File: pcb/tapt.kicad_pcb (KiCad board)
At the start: 2 copper layers, 23.7 x 28.3 mm, 26 parts, among them SW1 SW_SPDT_XKB_DMx-xxxx-1, SW2 SW_SPST, U1 nRF52810-QCxx, Y1 32MHz

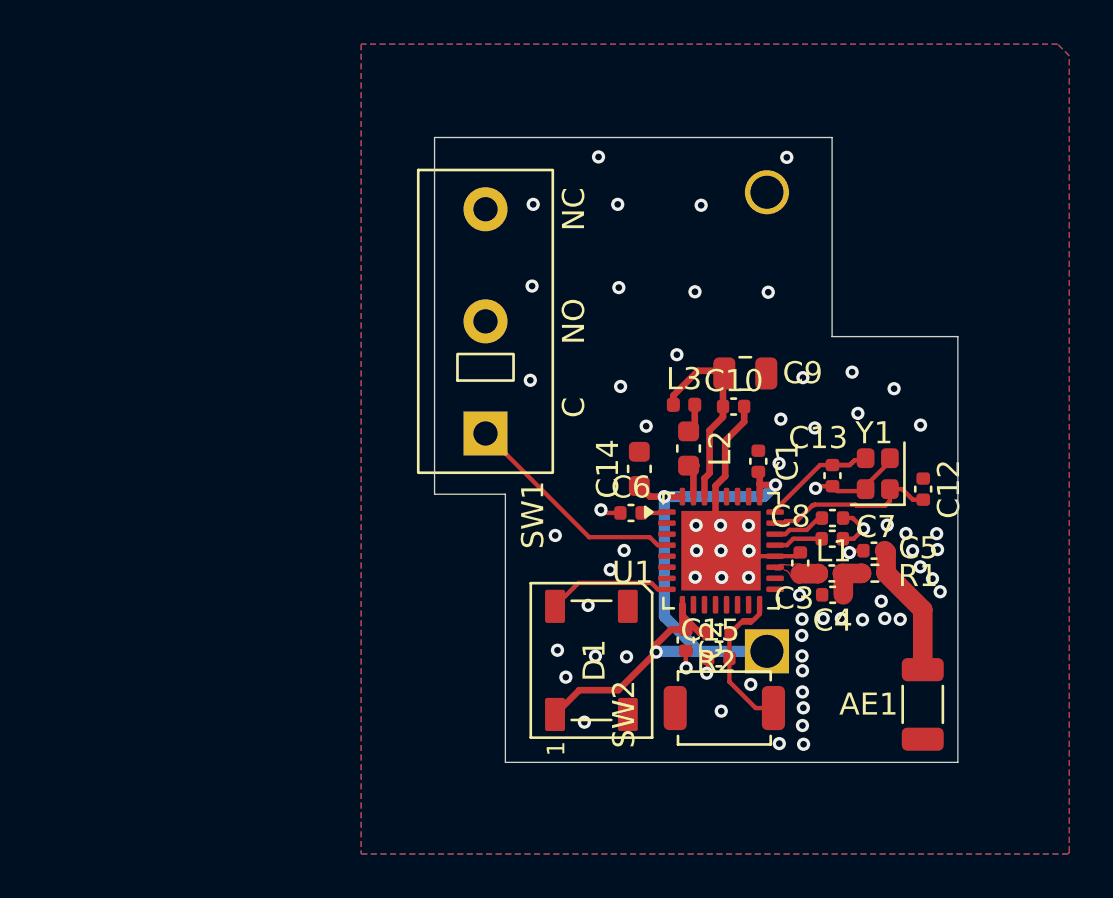
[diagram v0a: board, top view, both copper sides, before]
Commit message: major rf improvements, battery connector, component relayout
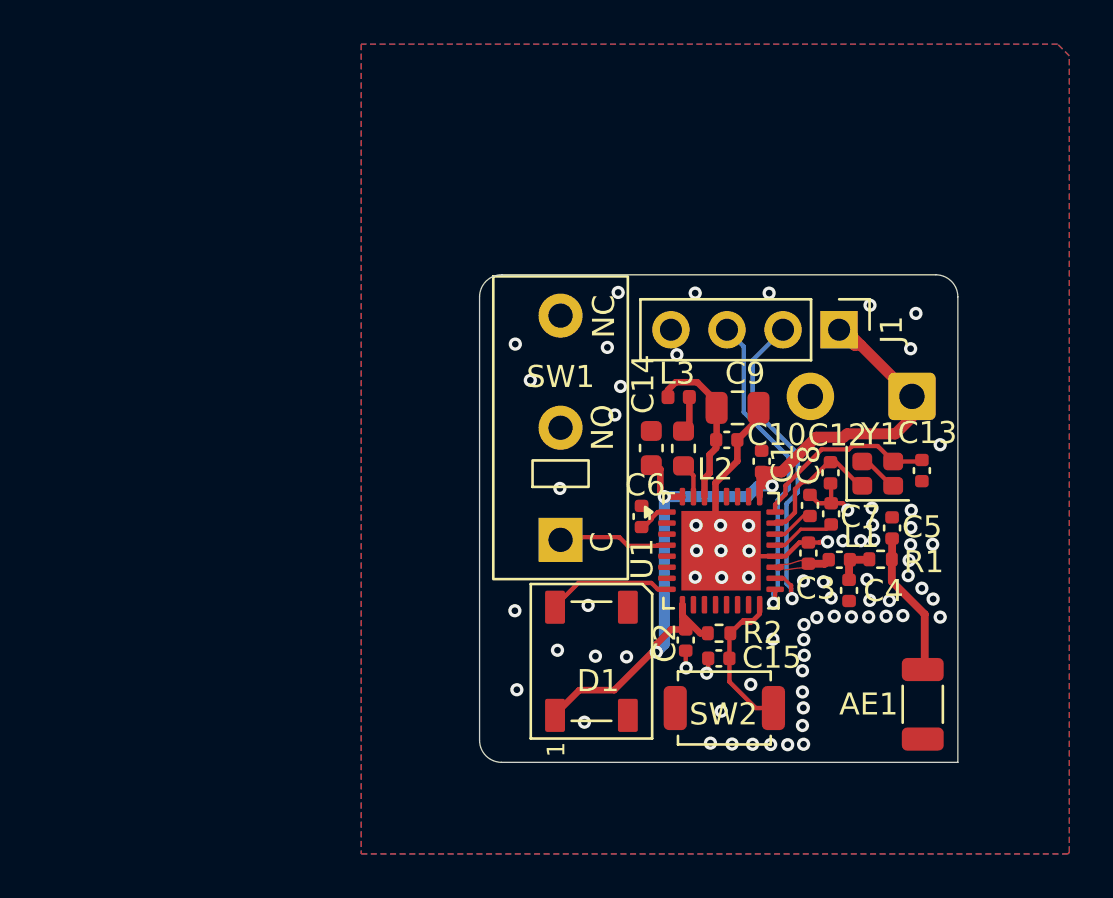
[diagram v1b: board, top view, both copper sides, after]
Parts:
- added J1: Conn_01x04_Pin, Connector_PinHeader_2.54mm:PinHeader_1x04_P2.54mm_Vertical, F.Cu at (103.5, 62.9)
- BT1: footprint Battery:BatteryHolder_MYOUNG_BS-07-A1BJ001_CR2032 -> Connector_Wire:SolderWire-0.5sqmm_1x02_P4.6mm_D0.9mm_OD2.1mm
- L2: footprint Capacitor_SMD:C_0603_1608Metric -> Inductor_SMD:L_0603_1608Metric
- moved BT1 13.3 mm to (106.8, 65.9), turned to 180 degrees
- moved SW1 5.90 mm to (90.8, 72.4)
- moved C12 4.26 mm to (103.1, 69.3), turned to 90 degrees
- moved C13 4.06 mm to (107.2, 69.2)
- moved C9 1.60 mm to (98.8, 66.4)
- moved C10 1.54 mm to (98.4, 67.8)
- moved C5 1.32 mm to (105.8, 71.8), turned to 90 degrees
- moved C8 1.17 mm to (102.1, 70.8), turned to -90 degrees
- moved C7 1.13 mm to (103.1, 71.2), turned to -90 degrees
- moved C14 1.09 mm to (94.9, 68.2)
- moved C4 0.77 mm to (103.9, 74.7), turned to -90 degrees
- moved L1 0.71 mm to (103.5, 73.3)
- moved R1 0.68 mm to (105.3, 73.3)
- moved C3 0.58 mm to (102.1, 73.0)
- moved C6 0.51 mm to (94.5, 71.3), turned to -90 degrees
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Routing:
- net SWDIO: track 0.00 -> 15.4 mm, vias 0 -> 1
- net SWDCLK: track 0.00 -> 14.5 mm, vias 0 -> 1
- net VDD: track 33.6 -> 42.6 mm
- net LIMIT: track 10.3 -> 5.85 mm
- net Net-(U1-XC2): track 5.91 -> 8.64 mm
- net GND: track 20.8 -> 19.0 mm, vias 71 -> 76
- net Net-(U1-XC1): track 7.94 -> 6.26 mm
- net Net-(U1-DEC4): track 9.17 -> 7.57 mm
- net Net-(U1-DEC2): track 2.23 -> 2.93 mm
- net Net-(AE1-FEED): track 5.99 -> 6.65 mm
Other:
- board size 23.7 x 28.3 mm -> 21.7 x 22.1 mm

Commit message: add mounting holes on dogboned corners
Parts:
- added H1: MountingHole, MountingHole:MountingHole_2.7mm_M2.5, F.Cu at (86.8, 82.5)
- added H2: MountingHole, MountingHole:MountingHole_2.7mm_M2.5, F.Cu at (108.8, 60.5)
- moved D1 0.28 mm to (92.2, 77.6)
- moved SW1 0.27 mm to (90.8, 72.1)
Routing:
- net GND: track 19.0 -> 23.2 mm, vias 76 -> 89
- net VDD: track 42.6 -> 42.0 mm, vias 3 -> 4
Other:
- board size 21.7 x 22.1 mm -> 28.3 x 28.3 mm

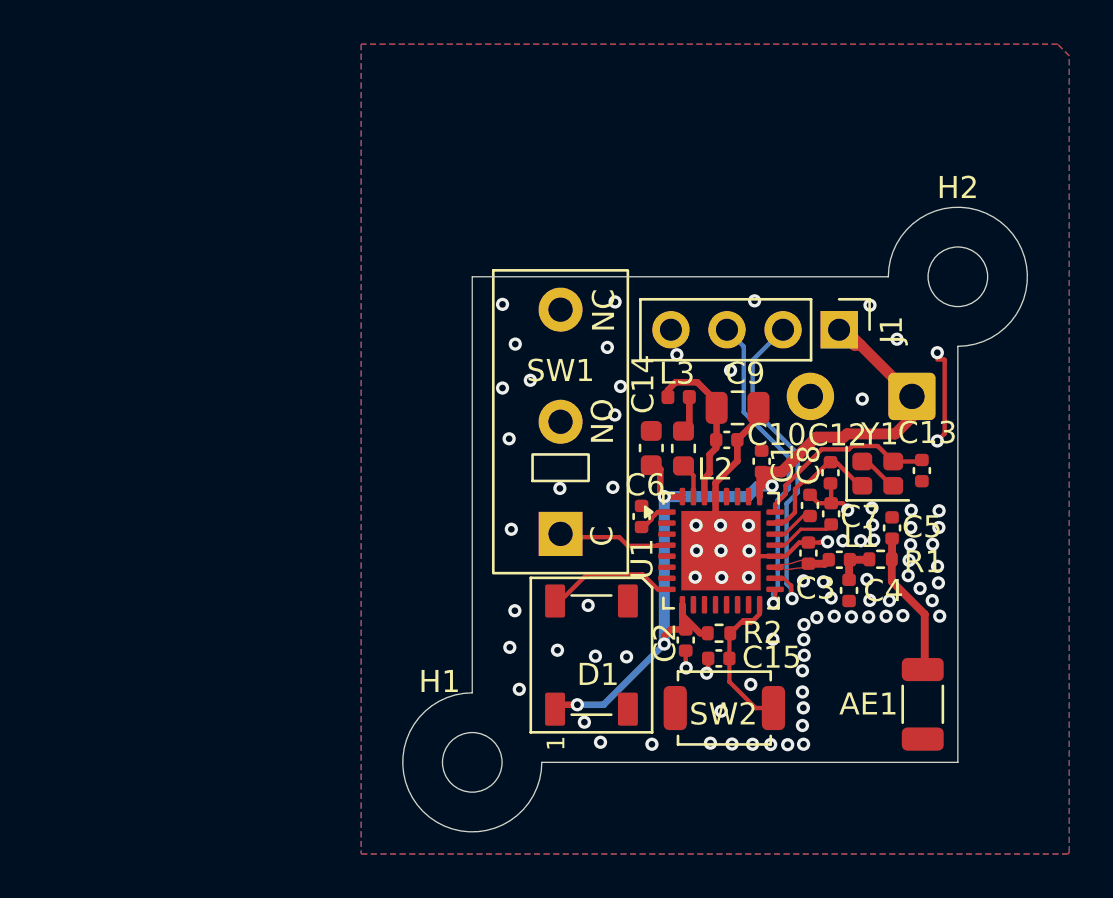
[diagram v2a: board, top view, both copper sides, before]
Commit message: pcb: silkscreen
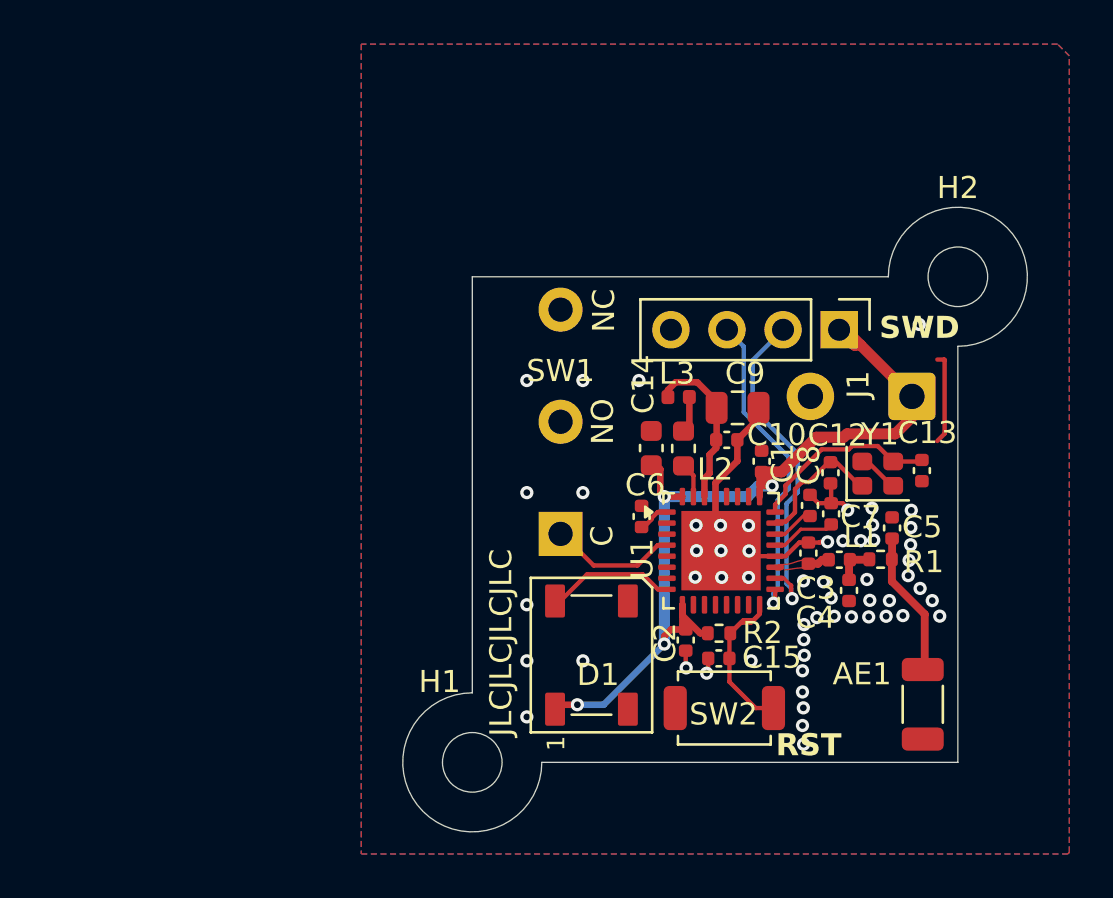
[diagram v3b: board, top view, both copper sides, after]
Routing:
- net LIMIT: track 5.85 -> 6.59 mm
- net GND: vias 89 -> 57
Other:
- board text added: "+"
- board text added: "-"
- board text added: "0123abc"
- board text added: "02/26"
- board text added: "JLCJLCJLCJLC"
- board text added: "RST"
- board text added: "SWD"
- board text added: "VDD IO CLK GND"
- board text added: "gh: grimsteel/tapt"
- board text added: "tapt v1"

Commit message: schematic: status led, uart
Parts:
- added D2: LED, LED_SMD:LED_0805_2012Metric, F.Cu at (69.2, 71.0)
- added J2: Conn_01x04_MountingPin, Connector_JST:JST_SH_BM04B-SRSS-TB_1x04-1MP_P1.00mm_Vertical, B.Cu at (94.2, 78.7)
- added R3: 1k, Resistor_SMD:R_0805_2012Metric, F.Cu at (73.6, 71.0)

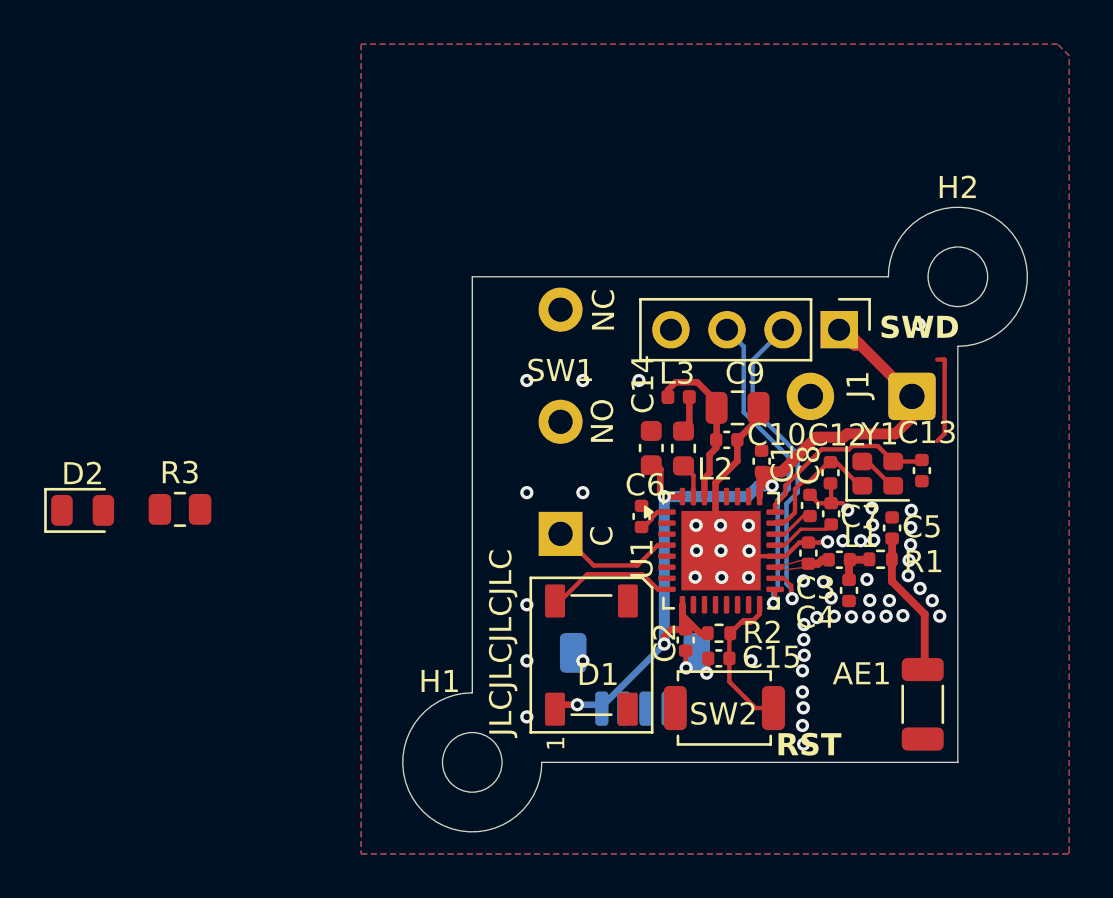
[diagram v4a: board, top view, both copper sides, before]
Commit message: pcb: uart, status led
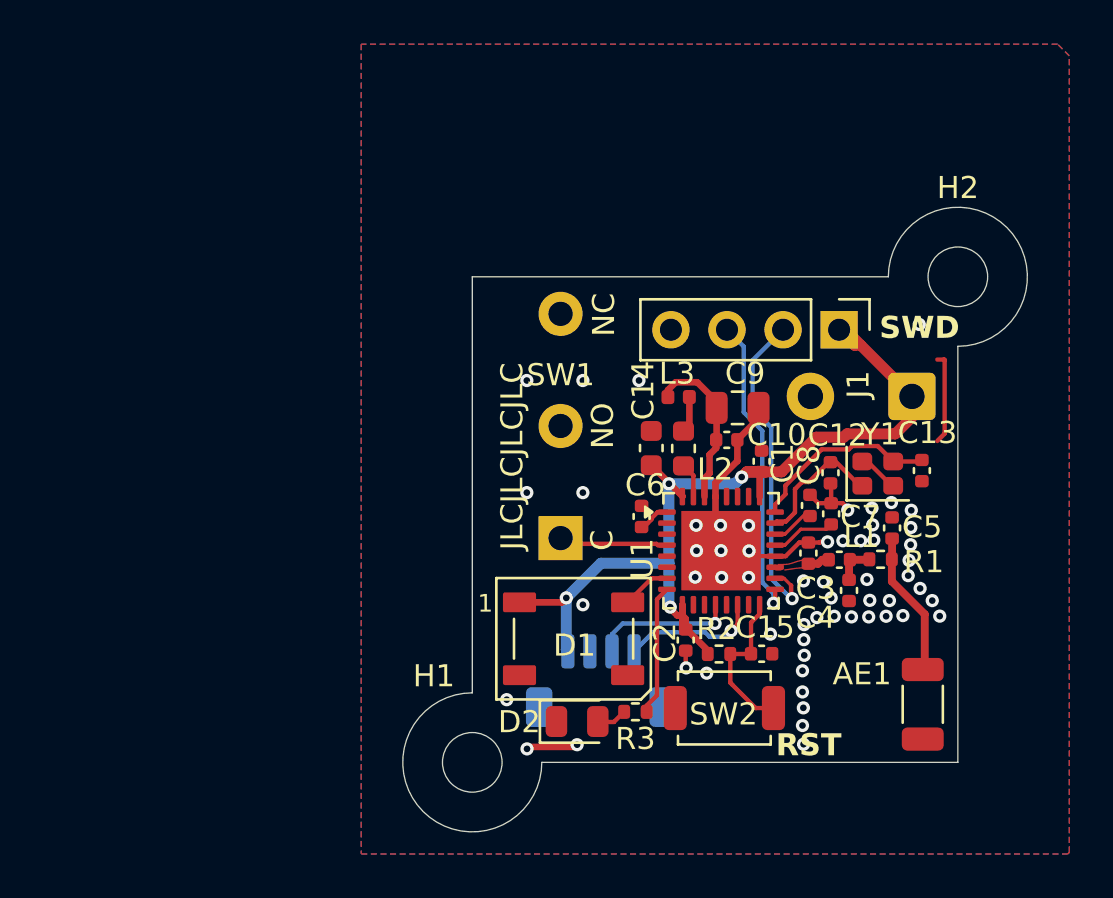
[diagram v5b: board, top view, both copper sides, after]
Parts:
- R3: footprint Resistor_SMD:R_0805_2012Metric -> Resistor_SMD:R_0402_1005Metric
- moved D2 24.4 mm to (91.6, 80.6)
- moved R3 22.6 mm to (94.2, 80.2)
- moved C15 1.95 mm to (99.9, 77.5), turned to 0 degrees
- moved J2 1.54 mm to (92.7, 78.8), turned to 0 degrees
- moved D1 1.10 mm to (91.4, 76.9), turned to 0 degrees
- moved R2 0.94 mm to (98.0, 77.5)
- moved SW1 0.19 mm to (90.8, 72.3)
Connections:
- U1 pad 12: unconnected-(U1-P0.15-Pad12) -> RX
- U1 pad 14: unconnected-(U1-P0.18-Pad14) -> TX
- U1 pad 7: unconnected-(U1-P0.09-Pad7) -> NEOPIXEL
- U1 pad 8: NEOPIXEL -> LED
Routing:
- net RX: track 0.00 -> 6.51 mm, vias 0 -> 1
- net TX: track 0.00 -> 6.25 mm, vias 0 -> 1
- net LED: track 0.00 -> 5.93 mm
- net NEOPIXEL: track 5.95 -> 2.23 mm
- net GND: track 23.2 -> 24.9 mm, vias 57 -> 58
- net RST: track 8.50 -> 7.06 mm
- net VDD: track 42.0 -> 43.4 mm
- net Net-(D2-A): track 0.00 -> 1.38 mm
- net LIMIT: track 6.59 -> 5.83 mm
- net SWDCLK: track 14.5 -> 13.9 mm
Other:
- board text added: "TX RX - +"

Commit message: pcb: 4 layer redesign, more antenna tuning, low freq crystal
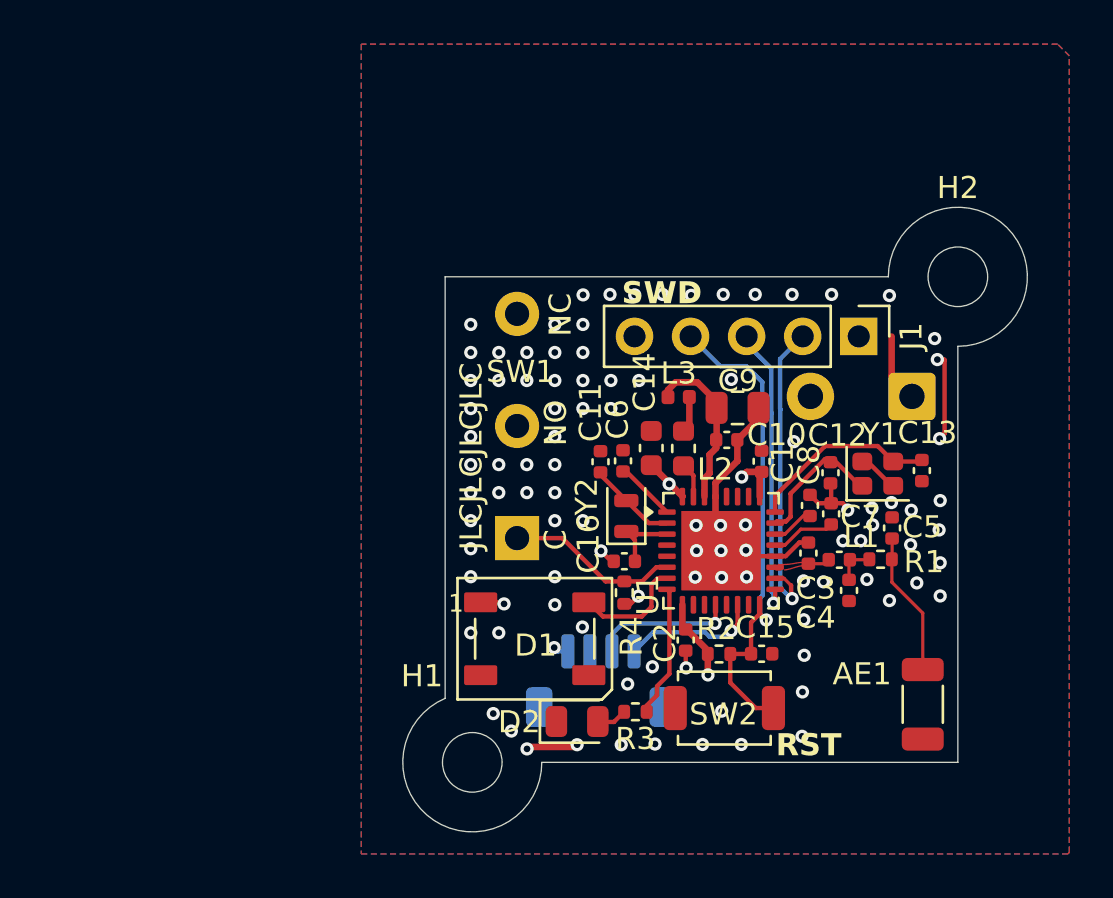
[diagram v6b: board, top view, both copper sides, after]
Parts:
- added C11: 12pF, Capacitor_SMD:C_0402_1005Metric, F.Cu at (92.6, 68.8)
- added C16: 12pF, Capacitor_SMD:C_0402_1005Metric, F.Cu at (93.7, 73.3)
- added R4: 100k, Resistor_SMD:R_0402_1005Metric, F.Cu at (93.7, 74.8)
- added Y2: 32.768kHz, Crystal:Crystal_SMD_2012-2Pin_2.0x1.2mm, F.Cu at (93.8, 71.3)
- J1: value Conn_01x04_Pin -> Conn_01x05_Pin; footprint Connector_PinHeader_2.54mm:PinHeader_1x04_P2.54mm_Vertical -> Connector_PinHeader_2.54mm:PinHeader_1x05_P2.54mm_Vertical
- R2: value 10k -> 100k
- SW1: value SW_SPDT_XKB_DMx-xxxx-1 -> SW_SPDT_LIMIT
- moved C6 2.66 mm to (93.7, 68.8)
- moved SW1 1.97 mm to (88.9, 72.3)
- moved D1 1.76 mm to (89.7, 76.9)
- moved J1 0.94 mm to (104.3, 63.2)
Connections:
- net Net-(U1-XC1) renamed XC1
- net Net-(U1-XC2) renamed XC2
- J1 pad 4: GND -> RST
- U1 pad 2: unconnected-(U1-P0.00/XL1-Pad2) -> XL1
- U1 pad 3: unconnected-(U1-P0.01/XL2-Pad3) -> XL2
- U1 pad 4: LIMIT -> unconnected-(U1-P0.04/AIN2-Pad4)
- U1 pad 6: unconnected-(U1-P0.06-Pad6) -> LIMIT
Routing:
- net VDD: track 43.4 -> 13.2 mm, vias 4 -> 6
- net RST: track 7.06 -> 22.9 mm, vias 0 -> 1
- net XL1: track 0.00 -> 4.03 mm
- net XL2: track 0.00 -> 3.40 mm
- net NEOPIXEL: track 2.23 -> 5.11 mm
- net LIMIT: track 5.83 -> 7.87 mm
- net GND: track 24.9 -> 23.1 mm, vias 58 -> 97
- net Net-(U1-DEC1): track 1.45 -> 2.75 mm
- net SWDIO: track 15.0 -> 14.0 mm
- net SWDCLK: track 13.9 -> 13.3 mm
- added copper zone on In1.Cu, net GND
- added copper zone on In2.Cu, net VDD
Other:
- outline, holes or cut-outs redrawn
- copper layers 2 -> 4
- board text added: "Stackup: JLC04161H-3313"
- board text added: "VDD IO CLK RST GND"
- board text removed: "VDD IO CLK GND"
